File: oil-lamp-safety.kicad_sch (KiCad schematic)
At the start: 29 parts, among them J1 Screw_Terminal_01x09, Q1 IRF540N, Q2 IRF540N, Q3 IRF540N, U1 HEF4093B

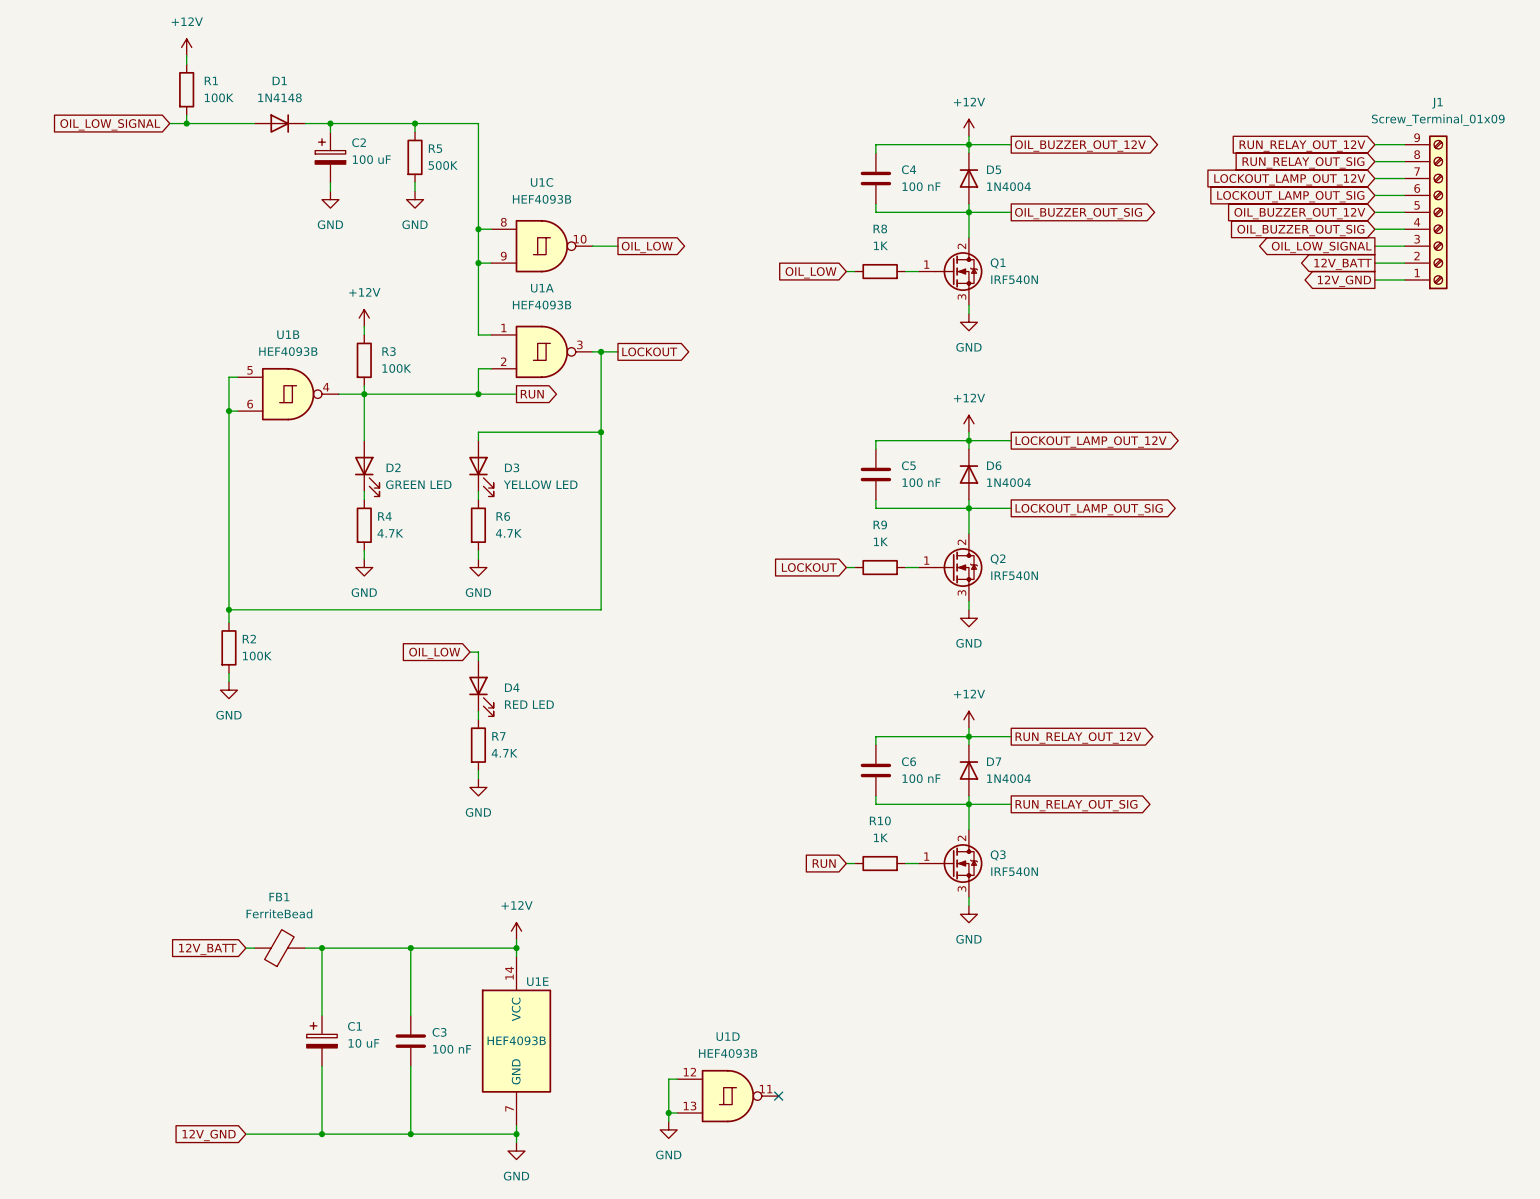
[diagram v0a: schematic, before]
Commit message: Updated the design to fix lockout on power up issue.
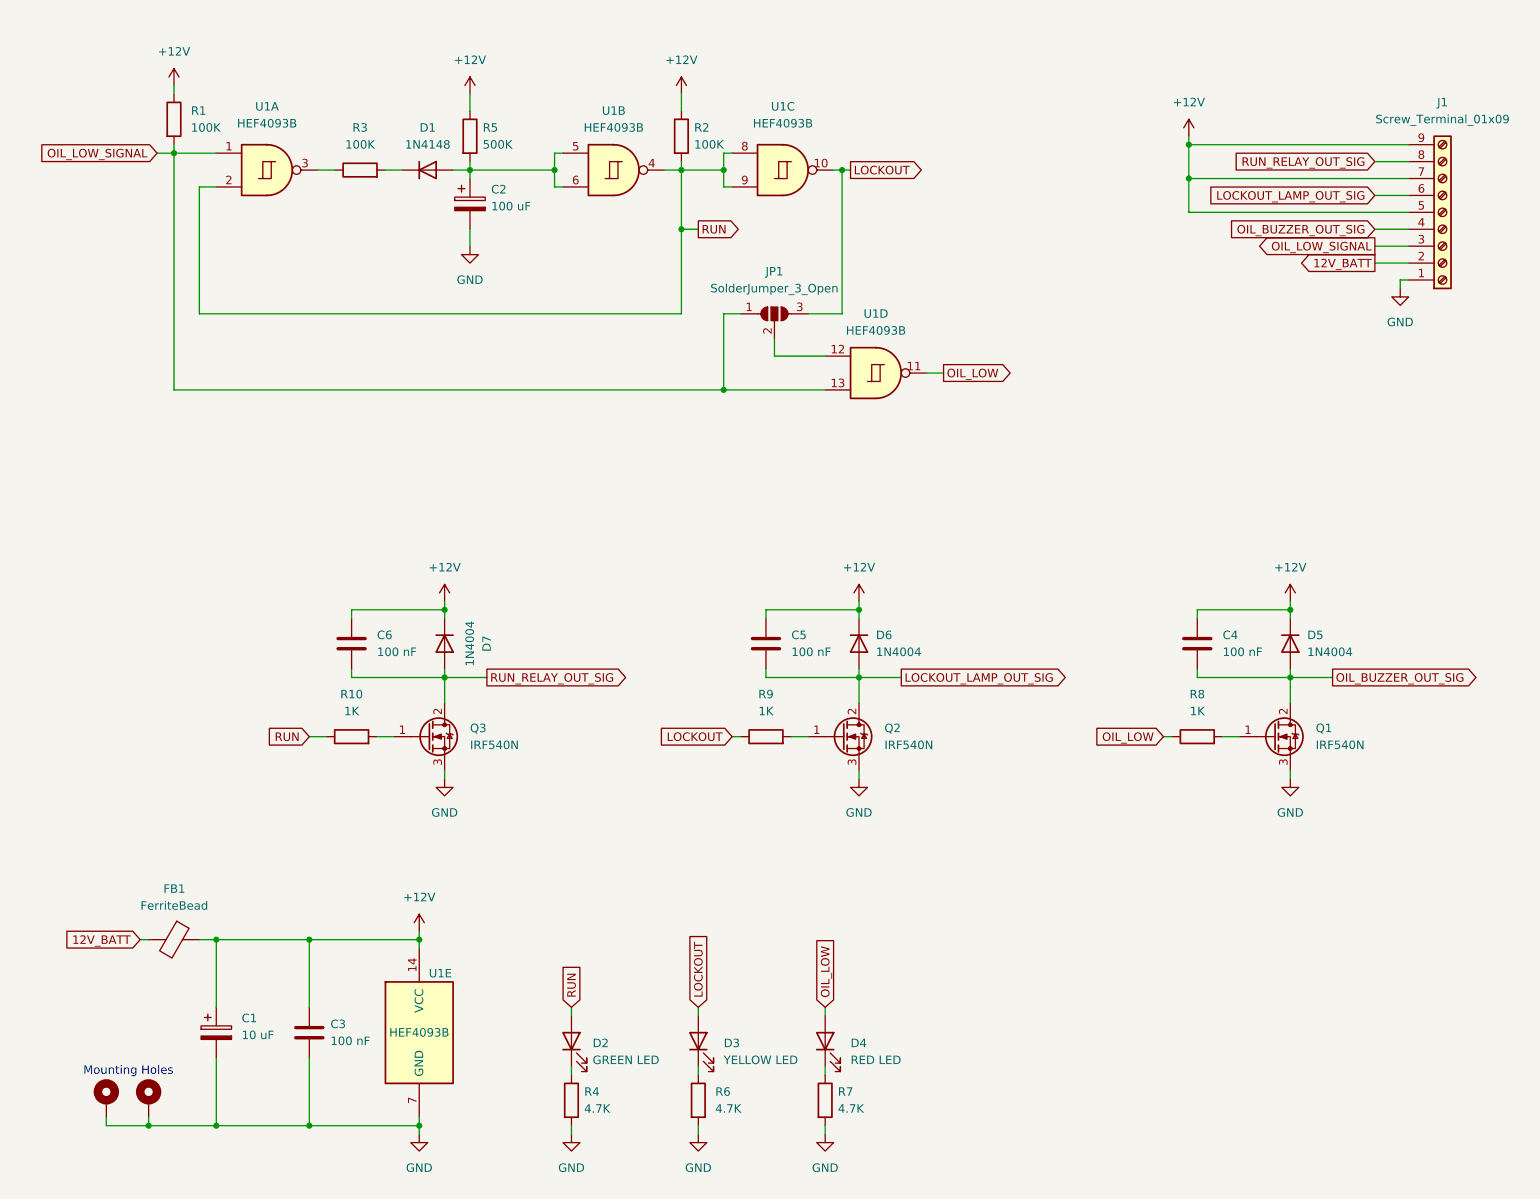
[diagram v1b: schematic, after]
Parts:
- added H1, H2: MountingHole_Pad, MountingHole:MountingHole_5.3mm_M5_Pad, symbol Mechanical:MountingHole_Pad
- added JP1: SolderJumper_3_Open, Jumper:SolderJumper-3_P1.3mm_Open_RoundedPad1.0x1.5mm, symbol Jumper:SolderJumper_3_Open
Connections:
- net +12V: now also FB1.1, R2.1, R5.1; no longer FB1.2, R3.1
- net 12V_BATT: now also FB1.2; no longer FB1.1
- net GND: now also H1.1, H2.1; no longer R2.2, R5.2, U1.12, U1.13
- net LOCKOUT: now also U1.10, JP1.3 (B); no longer R2.1, U1.3, U1.5, U1.6
- net OIL_LOW: now also U1.11; no longer U1.10
- net OIL_LOW_SIGNAL: now also U1.1, U1.13, JP1.1 (A); no longer D1.2 (A)
- net RUN: now also R2.2, U1.8, U1.9; no longer R3.2
- new net: JP1.2 (C), U1.12
- new net: C2.1, D1.2 (A), R5.2, U1.5, U1.6
- new net: D1.1 (K), R3.2
- new net: R3.1, U1.3
- no-connect marks 1 -> 0
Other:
- note added: "Mounting Holes"
- moved on the sheet: C1, C2, C3, C4, C5, C6, D2, D3, D4, FB1, J1, R1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
